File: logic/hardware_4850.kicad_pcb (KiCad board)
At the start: 4 copper layers, 84 x 79 mm, 203 parts, among them J101 PWM, J102 ADC, J1101 HALL, J1102 PWM_EN, J1103 CAN_IN, J1104 CAN_Out, J501 Enable, J601 AIN, J602 USB_B_Mini, J701 MOT_TEMP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

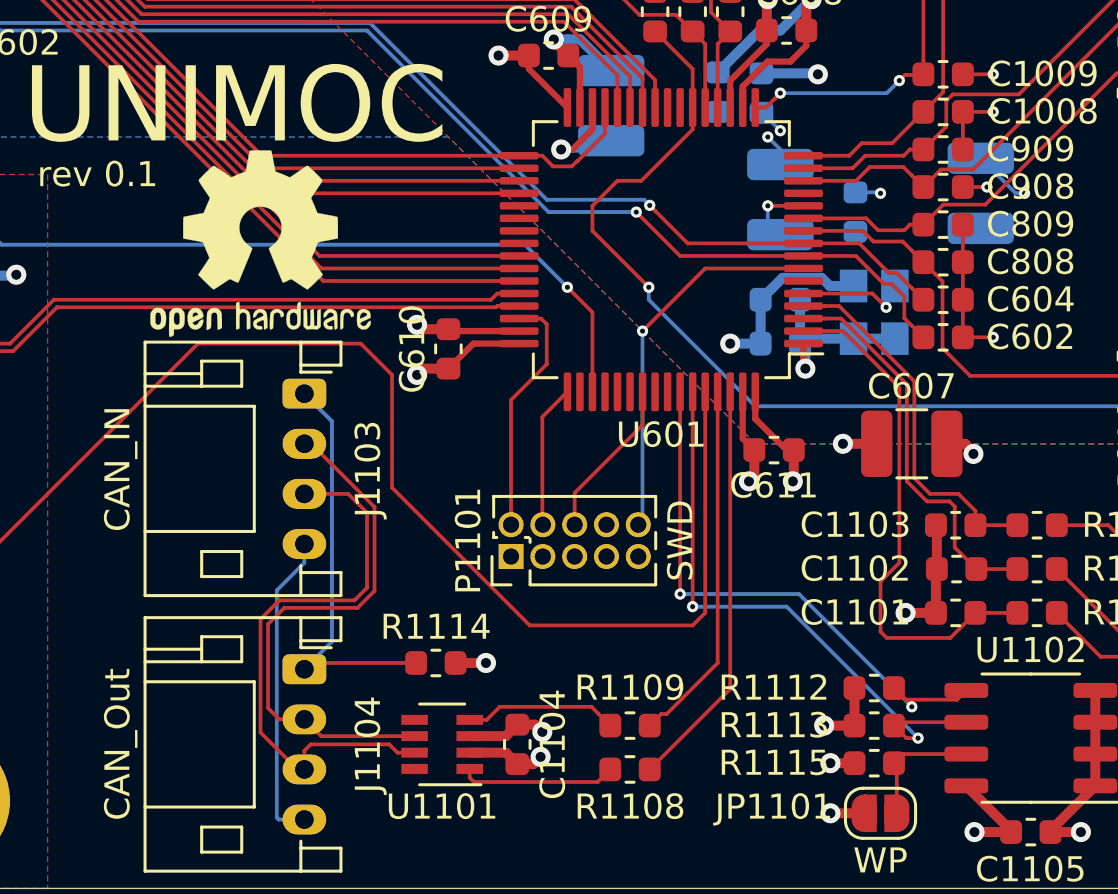
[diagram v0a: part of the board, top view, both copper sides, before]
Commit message: found the first error SDA and SCL swaped
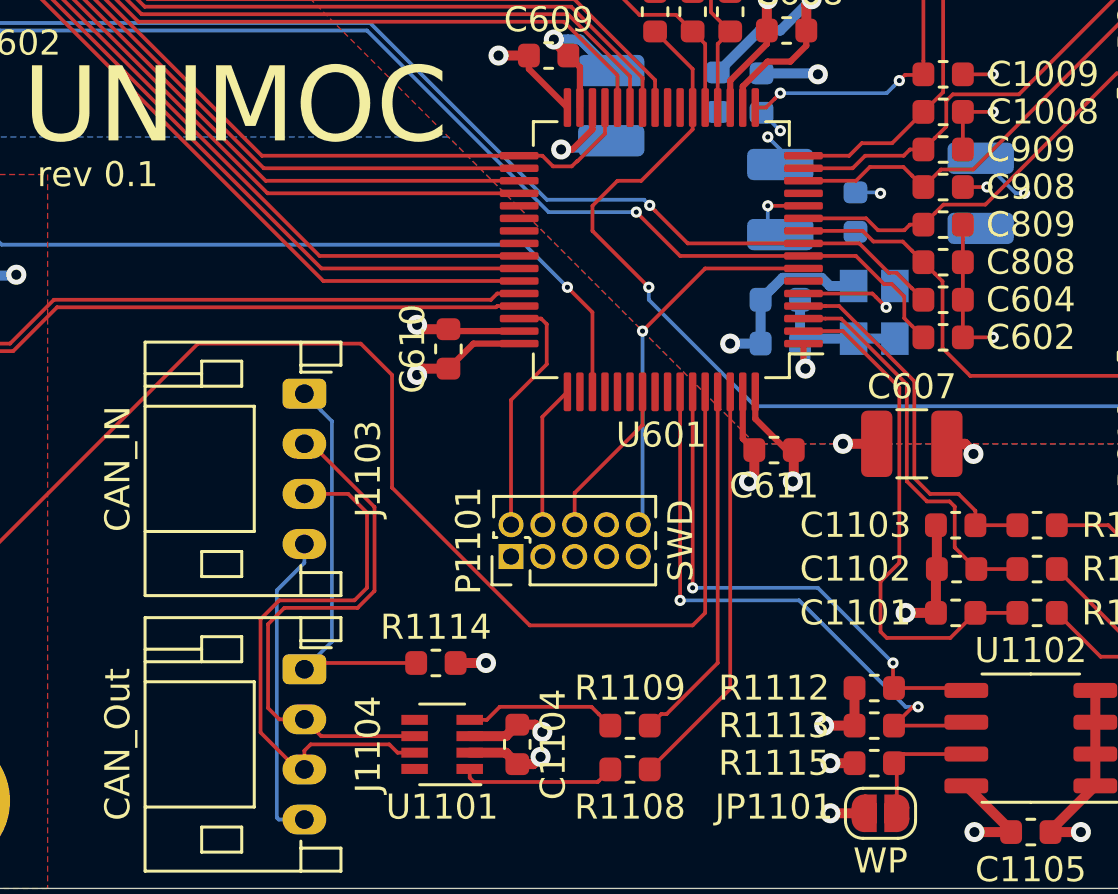
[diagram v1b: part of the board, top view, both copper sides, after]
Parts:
- removed REF**: OSHW-Logo2_9.8x8mm_SilkScreen, Symbol:OSHW-Logo2_9.8x8mm_SilkScreen
- C1001, C801, C901: value 100n -> 1n
- C1003, C803, C903: value 10n -> 100p
- C1004, C804, C904: value 10n -> 1n
- R1002, R802, R902: value 270R -> 47k
- R1005, R805, R905: value 100k -> 1M
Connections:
- J101 pad 3: Net-(J101-Pad3) -> (no net)
- J602 pad 4: Net-(J602-Pad4) -> (no net)
- P1101 pad 7: Net-(P1101-Pad7) -> (no net)
- P1101 pad 8: Net-(P1101-Pad8) -> (no net)
- P1101 pad 9: Net-(P1101-Pad9) -> (no net)
- R1112 pad 2: /controller/EEPROM_SCL -> /controller/EEPROM_SDA
- R1113 pad 2: /controller/EEPROM_SDA -> /controller/EEPROM_SCL
- U1101 pad 5: Net-(U1101-Pad5) -> (no net)
- U1101 pad 8: Net-(U1101-Pad8) -> (no net)
- U1102 pad 5: /controller/EEPROM_SCL -> /controller/EEPROM_SDA
- U1102 pad 6: /controller/EEPROM_SDA -> /controller/EEPROM_SCL
- U1103 pad 4: Net-(U1103-Pad4) -> (no net)
- U601 pad 23: Net-(U601-Pad23) -> (no net)
- U601 pad 24: Net-(U601-Pad24) -> (no net)
- U601 pad 37: Net-(U601-Pad37) -> (no net)
- U601 pad 38: Net-(U601-Pad38) -> (no net)
- U601 pad 39: Net-(U601-Pad39) -> (no net)
- U601 pad 40: Net-(U601-Pad40) -> (no net)
- U601 pad 50: Net-(U601-Pad50) -> (no net)
- U601 pad 52: Net-(U601-Pad52) -> (no net)
- U601 pad 53: Net-(U601-Pad53) -> (no net)
- U601 pad 54: Net-(U601-Pad54) -> (no net)
- U601 pad 56: Net-(U601-Pad56) -> (no net)
- U601 pad 57: Net-(U601-Pad57) -> (no net)
- U601 pad 6: Net-(U601-Pad6) -> (no net)
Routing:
- net /controller/EEPROM_SDA: track 23.9 -> 21.0 mm

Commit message: second prototype dimensioning
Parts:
- C1001, C1002, C703, C704, C801, C802, C901, C902: value 1n -> 10n
- C1004, C804, C904: value 1n -> 100n
- C1005, C705, C706, C805, C905: value 100p -> 1n
- C1009, C809, C909: value 10n -> 100p
- R1002, R802, R902: value 47k -> 510R
- R1004, R706, R708, R804, R904: value 11k -> 47k
- R1005, R805, R905: value 1M -> 100k
- R513: value 910R -> 3k3
- R701: value 10k 0.1% -> 24k 0.1%
- R702: value 560R 0.1% -> 1k2 0.1%
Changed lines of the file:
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@@
   (layers
     (0 Top mixed)
-    (1 Inner_Top signal)
-    (2 Inner_Bottom power)
-    (31 Bottom power)
+    (1 Inner_Top signal hide)
+    (2 Inner_Bottom power hide)
+    (31 Bottom power hide)
     (32 B.Adhes user)
     (33 F.Adhes user)
@@
     (solder_mask_min_width 0.25)
     (aux_axis_origin 0 0)
-    (visible_elements 7FFDFFFF)
+    (visible_elements 7FFCFFFF)
     (pcbplotparams
       (layerselection 0x010f0_ffffffff)
@@
       (effects (font (size 1 1) (thickness 0.15)))
     )
-    (fp_text value 1M (at 0 1.43) (layer F.Fab)
+    (fp_text value 100k (at 0 1.43) (layer F.Fab)
       (effects (font (size 1 1) (thickness 0.15)))
     )
@@
       (effects (font (size 1 1) (thickness 0.15)))
     )
-    (fp_text value 11k (at 0 1.43) (layer F.Fab)
+    (fp_text value 47k (at 0 1.43) (layer F.Fab)
       (effects (font (size 1 1) (thickness 0.15)))
     )
@@
       (effects (font (size 1 1) (thickness 0.15)))
     )
-    (fp_text value 47k (at 0 1.43) (layer F.Fab)
+    (fp_text value 510R (at 0 1.43) (layer F.Fab)
       (effects (font (size 1 1) (thickness 0.15)))
     )
@@
       (effects (font (size 1 1) (thickness 0.15)))
     )
-    (fp_text value 1M (at 0 1.43) (layer F.Fab)
+    (fp_text value 100k (at 0 1.43) (layer F.Fab)
       (effects (font (size 1 1) (thickness 0.15)))
     )
@@
       (effects (font (size 1 1) (thickness 0.15)))
     )
-    (fp_text value 11k (at 0 1.43) (layer F.Fab)
+    (fp_text value 47k (at 0 1.43) (layer F.Fab)
       (effects (font (size 1 1) (thickness 0.15)))
     )
@@
       (effects (font (size 1 1) (thickness 0.15)))
     )
-    (fp_text value 47k (at 0 1.43) (layer F.Fab)
+    (fp_text value 510R (at 0 1.43) (layer F.Fab)
       (effects (font (size 1 1) (thickness 0.15)))
     )
@@
       (effects (font (size 1 1) (thickness 0.15)))
     )
-    (fp_text value 1M (at 0 1.43 90) (layer F.Fab)
+    (fp_text value 100k (at 0 1.43 90) (layer F.Fab)
       (effects (font (size 1 1) (thickness 0.15)))
     )
@@
       (effects (font (size 1 1) (thickness 0.15)))
     )
-    (fp_text value 11k (at 0 1.43 90) (layer F.Fab)
+    (fp_text value 47k (at 0 1.43 90) (layer F.Fab)
       (effects (font (size 1 1) (thickness 0.15)))
     )
@@
       (effects (font (size 1 1) (thickness 0.15)))
     )
-    (fp_text value 47k (at 0 1.43 90) (layer F.Fab)
+    (fp_text value 510R (at 0 1.43 90) (layer F.Fab)
       (effects (font (size 1 1) (thickness 0.15)))
     )
@@
       (effects (font (size 1 1) (thickness 0.15)))
     )
-    (fp_text value 11k (at 0 1.43) (layer F.Fab)
+    (fp_text value 47k (at 0 1.43) (layer F.Fab)
       (effects (font (size 1 1) (thickness 0.15)))
     )
@@
       (effects (font (size 1 1) (thickness 0.15)))
     )
-    (fp_text value 11k (at 0 1.43) (layer F.Fab)
+    (fp_text value 47k (at 0 1.43) (layer F.Fab)
       (effects (font (size 1 1) (thickness 0.15)))
     )
@@
       (effects (font (size 1 1) (thickness 0.15)))
     )
-    (fp_text value "560R 0.1%" (at 0 1.43) (layer F.Fab)
+    (fp_text value "1k2 0.1%" (at 0 1.43) (layer F.Fab)
       (effects (font (size 1 1) (thickness 0.15)))
     )
@@
       (effects (font (size 1 1) (thickness 0.15)))
     )
-    (fp_text value "10k 0.1%" (at 0 1.43) (layer F.Fab)
+    (fp_text value "24k 0.1%" (at 0 1.43) (layer F.Fab)
       (effects (font (size 1 1) (thickness 0.15)))
     )
@@
       (effects (font (size 1 1) (thickness 0.15)))
     )
-    (fp_text value 910R (at 0 1.43 90) (layer F.Fab)
+    (fp_text value 3k3 (at 0 1.43 90) (layer F.Fab)
       (effects (font (size 1 1) (thickness 0.15)))
     )
@@
       (effects (font (size 1 1) (thickness 0.15)))
     )
-    (fp_text value 10n (at 0 1.43) (layer F.Fab)
+    (fp_text value 100p (at 0 1.43) (layer F.Fab)
       (effects (font (size 1 1) (thickness 0.15)))
     )
@@
       (effects (font (size 1 1) (thickness 0.15)))
     )
-    (fp_text value 100p (at 0 1.43) (layer F.Fab)
+    (fp_text value 1n (at 0 1.43) (layer F.Fab)
       (effects (font (size 1 1) (thickness 0.15)))
     )
@@
       (effects (font (size 1 1) (thickness 0.15)))
     )
-    (fp_text value 1n (at 0 1.43) (layer F.Fab)
+    (fp_text value 100n (at 0 1.43) (layer F.Fab)
       (effects (font (size 1 1) (thickness 0.15)))
     )
@@
       (effects (font (size 1 1) (thickness 0.15)))
     )
-    (fp_text value 1n (at 0 1.43) (layer F.Fab)
+    (fp_text value 10n (at 0 1.43) (layer F.Fab)
       (effects (font (size 1 1) (thickness 0.15)))
     )
@@
       (effects (font (size 1 1) (thickness 0.15)))
     )
-    (fp_text value 1n (at 0 1.43) (layer F.Fab)
+    (fp_text value 10n (at 0 1.43) (layer F.Fab)
       (effects (font (size 1 1) (thickness 0.15)))
     )
@@
       (effects (font (size 1 1) (thickness 0.15)))
     )
-    (fp_text value 10n (at 0 1.43) (layer F.Fab)
+    (fp_text value 100p (at 0 1.43) (layer F.Fab)
       (effects (font (size 1 1) (thickness 0.15)))
     )
@@
       (effects (font (size 1 1) (thickness 0.15)))
     )
-    (fp_text value 100p (at 0 1.43) (layer F.Fab)
+    (fp_text value 1n (at 0 1.43) (layer F.Fab)
       (effects (font (size 1 1) (thickness 0.15)))
     )
@@
       (effects (font (size 1 1) (thickness 0.15)))
     )
-    (fp_text value 1n (at 0 1.43) (layer F.Fab)
+    (fp_text value 100n (at 0 1.43) (layer F.Fab)
       (effects (font (size 1 1) (thickness 0.15)))
     )
@@
       (effects (font (size 1 1) (thickness 0.15)))
     )
-    (fp_text value 1n (at 0 1.43) (layer F.Fab)
+    (fp_text value 10n (at 0 1.43) (layer F.Fab)
       (effects (font (size 1 1) (thickness 0.15)))
     )
@@
       (effects (font (size 1 1) (thickness 0.15)))
     )
-    (fp_text value 1n (at 0 1.43 180) (layer F.Fab)
+    (fp_text value 10n (at 0 1.43 180) (layer F.Fab)
       (effects (font (size 1 1) (thickness 0.15)))
     )
@@
       (effects (font (size 1 1) (thickness 0.15)))
     )
-    (fp_text value 10n (at 0 1.43) (layer F.Fab)
+    (fp_text value 100p (at 0 1.43) (layer F.Fab)
       (effects (font (size 1 1) (thickness 0.15)))
     )
@@
       (effects (font (size 1 1) (thickness 0.15)))
     )
-    (fp_text value 100p (at 0 1.43 90) (layer F.Fab)
+    (fp_text value 1n (at 0 1.43 90) (layer F.Fab)
       (effects (font (size 1 1) (thickness 0.15)))
     )
@@
       (effects (font (size 1 1) (thickness 0.15)))
     )
-    (fp_text value 1n (at 0 1.43 90) (layer F.Fab)
+    (fp_text value 100n (at 0 1.43 90) (layer F.Fab)
       (effects (font (size 1 1) (thickness 0.15)))
     )
@@
       (effects (font (size 1 1) (thickness 0.15)))
     )
-    (fp_text value 1n (at 0 1.43 90) (layer F.Fab)
+    (fp_text value 10n (at 0 1.43 90) (layer F.Fab)
       (effects (font (size 1 1) (thickness 0.15)))
     )
@@
       (effects (font (size 1 1) (thickness 0.15)))
     )
-    (fp_text value 1n (at 0 1.43 90) (layer F.Fab)
+    (fp_text value 10n (at 0 1.43 90) (layer F.Fab)
       (effects (font (size 1 1) (thickness 0.15)))
     )
@@
       (effects (font (size 1 1) (thickness 0.15)))
     )
-    (fp_text value 100p (at 0 1.43) (layer F.Fab)
+    (fp_text value 1n (at 0 1.43) (layer F.Fab)
       (effects (font (size 1 1) (thickness 0.15)))
     )
@@
       (effects (font (size 1 1) (thickness 0.15)))
     )
-    (fp_text value 100p (at 0 1.43) (layer F.Fab)
+    (fp_text value 1n (at 0 1.43) (layer F.Fab)
       (effects (font (size 1 1) (thickness 0.15)))
     )
@@
       (effects (font (size 1 1) (thickness 0.15)))
     )
-    (fp_text value 1n (at 0 1.43) (layer F.Fab)
+    (fp_text value 10n (at 0 1.43) (layer F.Fab)
       (effects (font (size 1 1) (thickness 0.15)))
     )
@@
       (effects (font (size 1 1) (thickness 0.15)))
     )
-    (fp_text value 1n (at 0 1.43) (layer F.Fab)
+    (fp_text value 10n (at 0 1.43) (layer F.Fab)
       (effects (font (size 1 1) (thickness 0.15)))
     )

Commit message: parts update
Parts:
- R1105: value 11k -> 510R
- R1112, R1113: value 11k -> 4k7
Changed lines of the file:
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@@
       (effects (font (size 1 1) (thickness 0.15)))
     )
-    (fp_text value 11k (at 0 1.43) (layer F.Fab)
+    (fp_text value 4k7 (at 0 1.43) (layer F.Fab)
       (effects (font (size 1 1) (thickness 0.15)))
     )
@@
       (effects (font (size 1 1) (thickness 0.15)))
     )
-    (fp_text value 11k (at 0 1.43) (layer F.Fab)
+    (fp_text value 4k7 (at 0 1.43) (layer F.Fab)
       (effects (font (size 1 1) (thickness 0.15)))
     )
@@
       (effects (font (size 1 1) (thickness 0.15)))
     )
-    (fp_text value 11k (at 0 1.43) (layer F.Fab)
-      (effects (font (size 1 1) (thickness 0.15)))
-    )
+    (fp_text value 510R (at 0 1.43) (layer F.Fab)
+      (effects (font (size 1 1) (thickness 0.15)))
+    )

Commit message: new current filters
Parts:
- C1001, C1002, C801, C802, C901, C902: value 10n -> 4n7
- C1003, C803, C903: value 100p -> 47p
- C1004, C804, C904: value 100n -> 4n7
- C1005, C805, C905: value 1n -> 47p
- R1001, R1003, R801, R803, R901, R903: value 4k7 -> 9k1
- R1002, R802, R902: value 510R -> 4k7
- R1004, R804, R904: value 47k -> 470k
- R1005, R805, R905: value 100k -> 910k
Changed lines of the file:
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@@
-(kicad_pcb (version 20171130) (host pcbnew "(5.1.4)-1")
+(kicad_pcb (version 20171130) (host pcbnew "(5.1.5)-3")
   (general
     (thickness 1.6)
@@
       (effects (font (size 1 1) (thickness 0.15)))
     )
-    (fp_text value 100k (at 0 1.43) (layer F.Fab)
+    (fp_text value 910k (at 0 1.43) (layer F.Fab)
       (effects (font (size 1 1) (thickness 0.15)))
     )
@@
       (effects (font (size 1 1) (thickness 0.15)))
     )
-    (fp_text value 47k (at 0 1.43) (layer F.Fab)
+    (fp_text value 470k (at 0 1.43) (layer F.Fab)
       (effects (font (size 1 1) (thickness 0.15)))
     )
@@
       (effects (font (size 1 1) (thickness 0.15)))
     )
-    (fp_text value 4k7 (at 0 1.43) (layer F.Fab)
+    (fp_text value 9k1 (at 0 1.43) (layer F.Fab)
       (effects (font (size 1 1) (thickness 0.15)))
     )
@@
       (effects (font (size 1 1) (thickness 0.15)))
     )
-    (fp_text value 510R (at 0 1.43) (layer F.Fab)
+    (fp_text value 4k7 (at 0 1.43) (layer F.Fab)
       (effects (font (size 1 1) (thickness 0.15)))
     )
@@
       (effects (font (size 1 1) (thickness 0.15)))
     )
-    (fp_text value 4k7 (at 0 1.43) (layer F.Fab)
+    (fp_text value 9k1 (at 0 1.43) (layer F.Fab)
       (effects (font (size 1 1) (thickness 0.15)))
     )
@@
       (effects (font (size 1 1) (thickness 0.15)))
     )
-    (fp_text value 100k (at 0 1.43) (layer F.Fab)
+    (fp_text value 910k (at 0 1.43) (layer F.Fab)
       (effects (font (size 1 1) (thickness 0.15)))
     )
@@
       (effects (font (size 1 1) (thickness 0.15)))
     )
-    (fp_text value 47k (at 0 1.43) (layer F.Fab)
+    (fp_text value 470k (at 0 1.43) (layer F.Fab)
       (effects (font (size 1 1) (thickness 0.15)))
     )
@@
       (effects (font (size 1 1) (thickness 0.15)))
     )
-    (fp_text value 4k7 (at 0 1.43) (layer F.Fab)
+    (fp_text value 9k1 (at 0 1.43) (layer F.Fab)
       (effects (font (size 1 1) (thickness 0.15)))
     )
@@
       (effects (font (size 1 1) (thickness 0.15)))
     )
-    (fp_text value 510R (at 0 1.43) (layer F.Fab)
+    (fp_text value 4k7 (at 0 1.43) (layer F.Fab)
       (effects (font (size 1 1) (thickness 0.15)))
     )
@@
       (effects (font (size 1 1) (thickness 0.15)))
     )
-    (fp_text value 4k7 (at 0 1.43) (layer F.Fab)
+    (fp_text value 9k1 (at 0 1.43) (layer F.Fab)
       (effects (font (size 1 1) (thickness 0.15)))
     )
@@
       (effects (font (size 1 1) (thickness 0.15)))
     )
-    (fp_text value 100k (at 0 1.43 90) (layer F.Fab)
+    (fp_text value 910k (at 0 1.43 90) (layer F.Fab)
       (effects (font (size 1 1) (thickness 0.15)))
     )
@@
       (effects (font (size 1 1) (thickness 0.15)))
     )
-    (fp_text value 47k (at 0 1.43 90) (layer F.Fab)
+    (fp_text value 470k (at 0 1.43 90) (layer F.Fab)
       (effects (font (size 1 1) (thickness 0.15)))
     )
@@
       (effects (font (size 1 1) (thickness 0.15)))
     )
-    (fp_text value 4k7 (at 0 1.43 90) (layer F.Fab)
+    (fp_text value 9k1 (at 0 1.43 90) (layer F.Fab)
       (effects (font (size 1 1) (thickness 0.15)))
     )
@@
       (effects (font (size 1 1) (thickness 0.15)))
     )
-    (fp_text value 510R (at 0 1.43 90) (layer F.Fab)
+    (fp_text value 4k7 (at 0 1.43 90) (layer F.Fab)
       (effects (font (size 1 1) (thickness 0.15)))
     )
@@
       (effects (font (size 1 1) (thickness 0.15)))
     )
-    (fp_text value 4k7 (at 0 1.43 90) (layer F.Fab)
+    (fp_text value 9k1 (at 0 1.43 90) (layer F.Fab)
       (effects (font (size 1 1) (thickness 0.15)))
     )
@@
       (effects (font (size 1 1) (thickness 0.15)))
     )
-    (fp_text value 1n (at 0 1.43) (layer F.Fab)
+    (fp_text value 47p (at 0 1.43) (layer F.Fab)
       (effects (font (size 1 1) (thickness 0.15)))
     )
@@
       (effects (font (size 1 1) (thickness 0.15)))
     )
-    (fp_text value 100n (at 0 1.43) (layer F.Fab)
+    (fp_text value 4n7 (at 0 1.43) (layer F.Fab)
       (effects (font (size 1 1) (thickness 0.15)))
     )
@@
       (effects (font (size 1 1) (thickness 0.15)))
     )
-    (fp_text value 100p (at 0 1.43) (layer F.Fab)
+    (fp_text value 47p (at 0 1.43) (layer F.Fab)
       (effects (font (size 1 1) (thickness 0.15)))
     )
@@
       (effects (font (size 1 1) (thickness 0.15)))
     )
-    (fp_text value 10n (at 0 1.43) (layer F.Fab)
+    (fp_text value 4n7 (at 0 1.43) (layer F.Fab)
       (effects (font (size 1 1) (thickness 0.15)))
     )
@@
       (effects (font (size 1 1) (thickness 0.15)))
     )
-    (fp_text value 10n (at 0 1.43) (layer F.Fab)
+    (fp_text value 4n7 (at 0 1.43) (layer F.Fab)
       (effects (font (size 1 1) (thickness 0.15)))
     )
@@
       (effects (font (size 1 1) (thickness 0.15)))
     )
-    (fp_text value 1n (at 0 1.43) (layer F.Fab)
+    (fp_text value 47p (at 0 1.43) (layer F.Fab)
       (effects (font (size 1 1) (thickness 0.15)))
     )
@@
       (effects (font (size 1 1) (thickness 0.15)))
     )
-    (fp_text value 100n (at 0 1.43) (layer F.Fab)
+    (fp_text value 4n7 (at 0 1.43) (layer F.Fab)
       (effects (font (size 1 1) (thickness 0.15)))
     )
@@
       (effects (font (size 1 1) (thickness 0.15)))
     )
-    (fp_text value 100p (at 0 1.43) (layer F.Fab)
+    (fp_text value 47p (at 0 1.43) (layer F.Fab)
       (effects (font (size 1 1) (thickness 0.15)))
     )
@@
       (effects (font (size 1 1) (thickness 0.15)))
     )
-    (fp_text value 10n (at 0 1.43) (layer F.Fab)
+    (fp_text value 4n7 (at 0 1.43) (layer F.Fab)
       (effects (font (size 1 1) (thickness 0.15)))
     )
@@
       (effects (font (size 1 1) (thickness 0.15)))
     )
-    (fp_text value 10n (at 0 1.43 180) (layer F.Fab)
+    (fp_text value 4n7 (at 0 1.43 180) (layer F.Fab)
       (effects (font (size 1 1) (thickness 0.15)))
     )
@@
       (effects (font (size 1 1) (thickness 0.15)))
     )
-    (fp_text value 1n (at 0 1.43 90) (layer F.Fab)
+    (fp_text value 47p (at 0 1.43 90) (layer F.Fab)
       (effects (font (size 1 1) (thickness 0.15)))
     )
@@
       (effects (font (size 1 1) (thickness 0.15)))
     )
-    (fp_text value 100n (at 0 1.43 90) (layer F.Fab)
+    (fp_text value 4n7 (at 0 1.43 90) (layer F.Fab)
       (effects (font (size 1 1) (thickness 0.15)))
     )
@@
       (effects (font (size 1 1) (thickness 0.15)))
     )
-    (fp_text value 100p (at 0 1.43 90) (layer F.Fab)
+    (fp_text value 47p (at 0 1.43 90) (layer F.Fab)
       (effects (font (size 1 1) (thickness 0.15)))
     )
@@
       (effects (font (size 1 1) (thickness 0.15)))
     )
-    (fp_text value 10n (at 0 1.43 90) (layer F.Fab)
+    (fp_text value 4n7 (at 0 1.43 90) (layer F.Fab)
       (effects (font (size 1 1) (thickness 0.15)))
     )
@@
       (effects (font (size 1 1) (thickness 0.15)))
     )
-    (fp_text value 10n (at 0 1.43 90) (layer F.Fab)
+    (fp_text value 4n7 (at 0 1.43 90) (layer F.Fab)
       (effects (font (size 1 1) (thickness 0.15)))
     )

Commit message: fixed pwm_en bug
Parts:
- R1101: value 11k -> 510R
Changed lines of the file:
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@@
       (effects (font (size 1 1) (thickness 0.15)))
     )
-    (fp_text value 11k (at 0 1.43) (layer F.Fab)
+    (fp_text value 510R (at 0 1.43) (layer F.Fab)
       (effects (font (size 1 1) (thickness 0.15)))
     )
